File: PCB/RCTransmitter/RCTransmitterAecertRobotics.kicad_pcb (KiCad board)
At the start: 2 copper layers, 141.6 x 101.5 mm, 41 parts, among them J5019_1 J5019 Charger, K1 KCD1 Power Switch, P1 PCF8575

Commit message: updated new design
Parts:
- 10k_Potentiometer1: renamed from ‎PTV09A_1; value R_Potentiometer -> PTV09A-4220F-B103
- 10k_Potentiometer2: renamed from ‎PTV09A_2; value R_Potentiometer -> PTV09A-4220F-B103
- JST_Connector1: renamed from 1.27mm_JST_Connector_1; value Conn_01x02_Socket -> 1.27mm_JST_Connector_1
- Level_Shifter1: renamed from TXS0108E_1; value Level Shifter TXS0108EPW -> TXS0108EPW
- NRF24: renamed from NRF24L01+PA+LNA1; value NRF24L01 -> NRF24L01+PA+LNA1
- Rotary_Encoder1: renamed from EC11E_1; value RotaryEncoder_Switch -> EC11E
- Touch_Screen1: renamed from ILI9488_1; value Screen ILI9488 -> Hosyond 3.5 Inch TFT Touch Screen ILI9488
- moved H8 3.10 mm to (166.4, 67.3)
- renumbered HT7333-A_1 to 3.3V_Regulator1, J5019_1 to Battery_Charger1, KW12_1 to Bumper1, KW12_3 to Bumper2, KW12_2 to Bumper3, KW12_4 to Bumper4, Tact_Push_Button_1 to Button1, Tact_Push_Button_2 to Button2, Tact_Push_Button_3 to Button3, Tact_Push_Button_4 to Button4, MPU6050_1 to Gyroscope1, P1 to IO_Extender1, THB001P_1 to Joystick1, THB001P_2 to Joystick2, SPST_6A_Toggle_Switch_1 to Toggle_Switch1, SPST_6A_Toggle_Switch_2 to Toggle_Switch2, SPST_6A_Toggle_Switch_3 to Toggle_Switch3, SPST_6A_Toggle_Switch_4 to Toggle_Switch4
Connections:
- net /Button A (P03) renamed /Button A
- net /Button B (P04) renamed /Button B
- net /Button C (P05) renamed /Button C
- net /Button D (P06) renamed /Button D
- net /Joy Left Button (P01) renamed /Joy Left Button
- net /Joy Right Button (P02) renamed /Joy Right Button
- net /Left Bumper A (P07) renamed /Left Bumper A
- net /Left Bumper B (P10) renamed /Left Bumper B
- net /Right Bumper A (P11) renamed /Right Bumper A
- net /Right Bumper B (P12) renamed /Right Bumper B
- net /Rotary Encoder Switch (P00) renamed /Rotary Encoder Switch
- net /TFT Reset (D10) renamed /TFT Reset
- net /Toggle A (P13) renamed /Toggle A
- net /Toggle B (P14) renamed /Toggle B
- net /Toggle C (P15) renamed /Toggle C
- net /Toggle D (P16) renamed /Toggle D
- Arduino_Nano_V3 pad 10: /TFT CS (D7) -> /TFT CS
- Arduino_Nano_V3 pad 11: /TFT DC (D8) -> /TFT DC
- Arduino_Nano_V3 pad 12: /Touch Screen CS (D9) -> /Touch Screen CS
- Arduino_Nano_V3 pad 14: /MOSI (D11) -> /MOSI
- Arduino_Nano_V3 pad 15: /MISO (D12) -> /MISO
- Arduino_Nano_V3 pad 16: /SCK (D13) -> /SCK
- Arduino_Nano_V3 pad 19: /Joy Left Y (A0) -> /Joy Left Y
- Arduino_Nano_V3 pad 20: /Joy Left X (A1) -> /Joy Left X
- Arduino_Nano_V3 pad 21: /Pot Left (A6) -> /Pot Left
- Arduino_Nano_V3 pad 22: /Joy Right X (A2) -> /Joy Right X
- Arduino_Nano_V3 pad 23: /SDA (A4) -> /SDA
- Arduino_Nano_V3 pad 24: /SCL (A5) -> /SCL
- Arduino_Nano_V3 pad 25: /Joy Right Y (A3) -> /Joy Right Y
- Arduino_Nano_V3 pad 26: /Pot Right (A7) -> /Pot Right
- Arduino_Nano_V3 pad 5: /RotaryEncoderA (D2) -> /RotaryEncoderA
- Arduino_Nano_V3 pad 6: /RotaryEncoderB (D3) -> /RotaryEncoderB
- Arduino_Nano_V3 pad 8: /NRF CSN (D5) -> /NRF CSN
- Arduino_Nano_V3 pad 9: /NRF CE (D6) -> /NRF CE
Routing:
- net /5v: track 610.6 -> 496.6 mm
- net /TFT Reset: track 112.2 -> 34.5 mm
- net /Pot Right (A7): track 48.3 -> 70.7 mm, vias 3 -> 0
- net /3.3v: track 163.8 -> 182.1 mm, vias 8 -> 6
- net /SDA (A4): track 111.8 -> 98.5 mm, vias 8 -> 6
- net /Pot Left (A6): track 75.8 -> 87.5 mm, vias 5 -> 0
- net /SCL (A5): track 109.4 -> 100.3 mm, vias 8 -> 6
- net /Toggle D: track 105.8 -> 114.3 mm
- net /Joy Left X (A1): track 117.2 -> 124.6 mm
- net /Toggle B: track 50.6 -> 43.5 mm
- net Net-(Battery_Charger1-BAT+): track 62.9 -> 68.5 mm
- net /SCK (D13): track 117.7 -> 122.1 mm, vias 6 -> 7
- net /Toggle A: track 57.6 -> 53.2 mm
- net /Joy Left Y (A0): track 117.1 -> 121.5 mm
- net /Joy Right Button: track 116.0 -> 118.9 mm
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
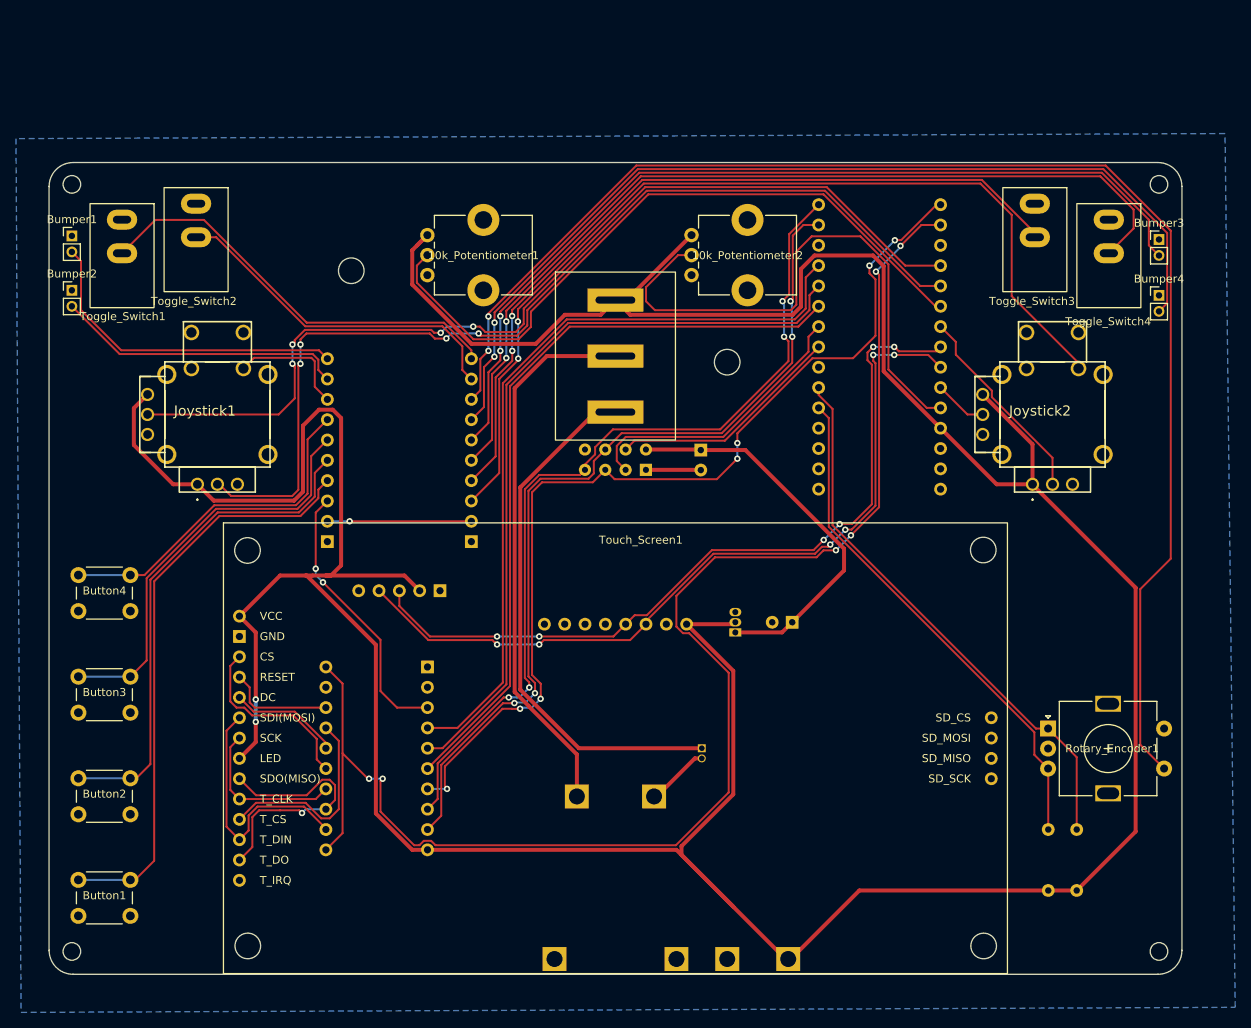
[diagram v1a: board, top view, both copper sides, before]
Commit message: nrf and screen not working at the same time
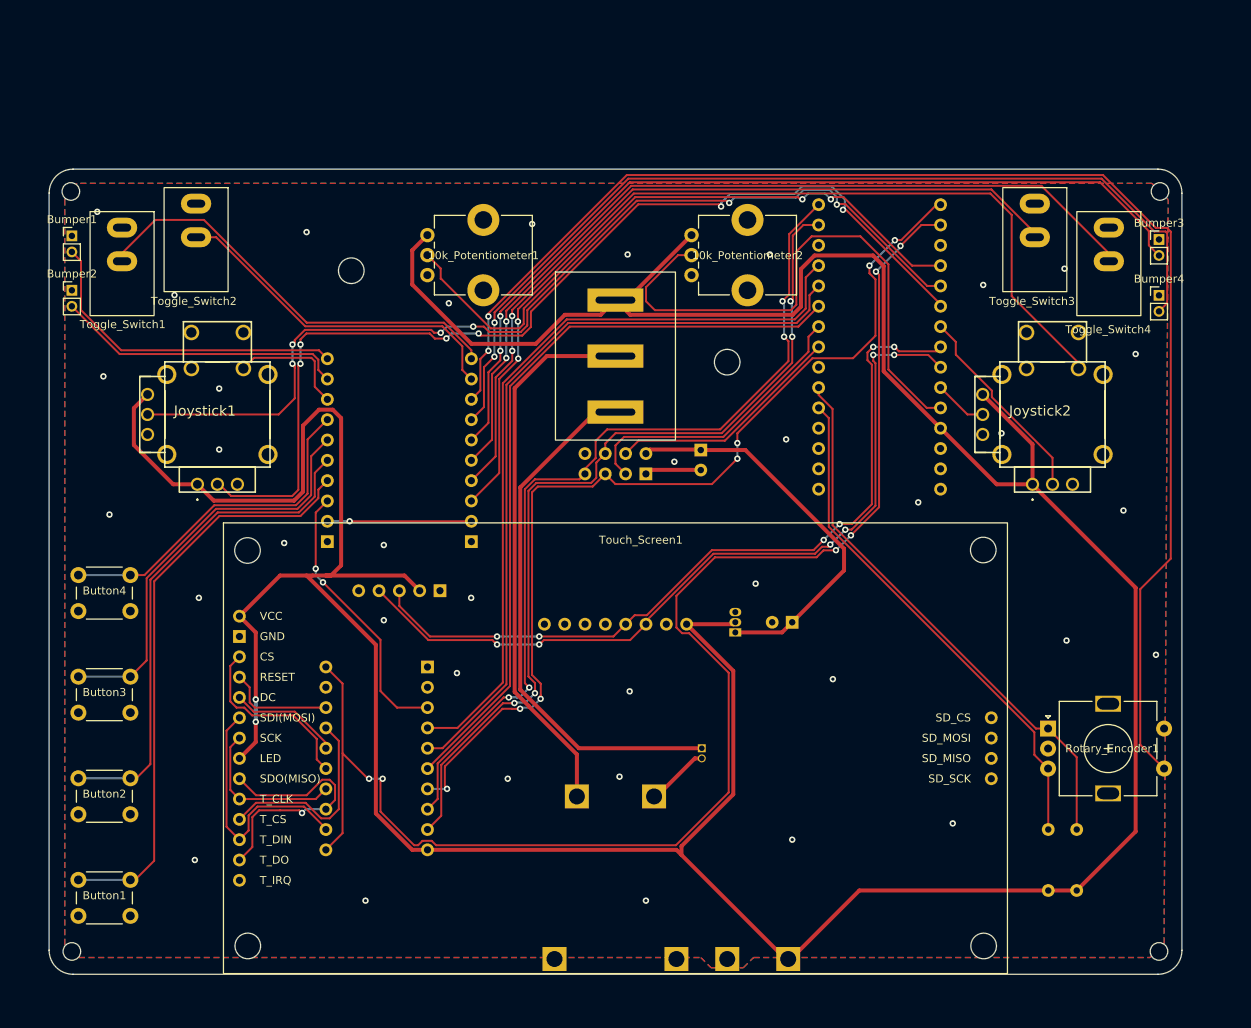
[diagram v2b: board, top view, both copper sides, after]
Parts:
- moved Toggle_Switch1 1.00 mm to (90.7, 48.5)
- moved Toggle_Switch4 1.00 mm to (214.1, 48.5)
- moved H2 0.90 mm to (220.5, 46.0)
- moved H1 0.90 mm to (84.3, 46.0)
- moved NRF24 0.51 mm to (156.2, 81.3)
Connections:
- 10k_Potentiometer1 pad 2: /Pot Left (A6) -> /Pot Left
- 10k_Potentiometer2 pad 2: /Pot Right (A7) -> /Pot Right
- Arduino_Nano_V3 pad 19: /Joy Left Y -> /Pot Left
- Arduino_Nano_V3 pad 20: /Joy Left X -> /Joy Left Y
- Arduino_Nano_V3 pad 21: /Pot Left -> /Joy Left X
- Joystick1 pad 12: /Joy Left Y (A0) -> /Joy Left Y
- Joystick1 pad 2: /Joy Left X (A1) -> /Joy Left X
- Joystick2 pad 12: /Joy Right Y (A3) -> /Joy Right Y
- Joystick2 pad 2: /Joy Right X (A2) -> /Joy Right X
- Level_Shifter1 pad 14: /Touch Screen CS (D9) -> /Touch Screen CS
- Level_Shifter1 pad 15: /TFT DC (D8) -> /TFT DC
- Level_Shifter1 pad 16: /TFT CS (D7) -> /TFT CS
- Level_Shifter1 pad 17: /SCK (D13) -> /SCK
- Level_Shifter1 pad 18: /MISO (D12) -> /MISO
- Level_Shifter1 pad 19: /MOSI (D11) -> /MOSI
- NRF24 pad 2: /NRF CSN (D5) -> /NRF CSN
- NRF24 pad 3: /MOSI (D11) -> /MOSI
- NRF24 pad 5: /MISO (D12) -> /MISO
- NRF24 pad 6: /SCK (D13) -> /SCK
- NRF24 pad 7: /NRF CE (D6) -> /NRF CE
- R10k_1 pad 2: /RotaryEncoderB (D3) -> /RotaryEncoderB
- R10k_2 pad 2: /RotaryEncoderA (D2) -> /RotaryEncoderA
- Rotary_Encoder1 pad A: /RotaryEncoderB (D3) -> /RotaryEncoderB
- Rotary_Encoder1 pad B: /RotaryEncoderA (D2) -> /RotaryEncoderA
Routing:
- net /Joy Left X: track 0.00 -> 127.8 mm, vias 0 -> 6
- net /Joy Left X (A1): track 124.6 -> 0.00 mm, vias 4 -> 0
- net /Joy Left Y: track 0.00 -> 123.0 mm, vias 0 -> 6
- net /SCK: track 0.00 -> 122.2 mm, vias 0 -> 7
- net /SCK (D13): track 122.1 -> 0.00 mm, vias 7 -> 0
- net /Joy Left Y (A0): track 121.5 -> 0.00 mm, vias 4 -> 0
- net /MOSI: track 0.00 -> 111.2 mm, vias 0 -> 4
- net /MOSI (D11): track 110.2 -> 0.00 mm, vias 4 -> 0
- net /MISO: track 0.00 -> 109.6 mm, vias 0 -> 4
- net /MISO (D12): track 108.9 -> 0.00 mm, vias 4 -> 0
- net /Touch Screen CS (D9): track 97.0 -> 0.00 mm
- net /Touch Screen CS: track 0.00 -> 97.0 mm
- net /TFT DC (D8): track 95.9 -> 0.00 mm
- net /TFT DC: track 0.00 -> 95.9 mm
- net /TFT CS (D7): track 94.8 -> 0.00 mm
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- added copper zone on F.Cu, net GND
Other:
- board size 141.6 x 101.5 mm -> 141.6 x 100.6 mm

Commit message: nrf stuff
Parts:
- removed Level_Shifter1: TXS0108EPW, AddedFootprints:HW-221 Level Shifter
- removed Touch_Screen1: Hosyond 3.5 Inch TFT Touch Screen ILI9488, AddedFootprints:3.5 Inch Screen SPI_Module_ILI9488
- added OLED_LCD_Display1: SSD1309 2.4inch, AddedFootprints:OLED LCD Display SSD1309, F.Cu at (116.9, 90.2)
- H1, H10, H2, H9: footprint MountingHole:MountingHole_2.2mm_M2 -> MountingHole:MountingHole_3.2mm_M3
- moved H6 100.7 mm to (219.7, 47.0)
- moved H10 91.4 mm to (168.9, 65.4)
- moved H9 91.1 mm to (135.3, 65.4)
- moved H8 83.8 mm to (85.1, 47.0)
- moved IO_Extender1 75.3 mm to (125.5, 139.9), turned to 0 degrees
- moved H1 57.5 mm to (118.7, 92.1)
- moved H2 57.5 mm to (186.1, 92.1)
- moved C10uf_3 46.8 mm to (135.0, 74.7), turned to 90 degrees
- moved Button1 43.4 mm to (113.1, 98.8)
- moved H5 42.6 mm to (118.9, 131.6)
- moved H7 42.5 mm to (186.1, 131.4)
- moved 3.3V_Regulator1 38.2 mm to (140.1, 74.3)
- moved Button4 37.5 mm to (113.1, 129.2)
- moved Button2 26.0 mm to (113.1, 108.9)
- moved Button3 22.8 mm to (113.1, 119.1)
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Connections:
- 10k_Potentiometer1 pad 3: /5v -> /REF
- 10k_Potentiometer2 pad 3: /5v -> /REF
- 3.3V_Regulator1 pad 2: /5v -> /Vin
- Arduino_Nano_V3 pad 10: /TFT CS -> /Screen RES
- Arduino_Nano_V3 pad 11: /TFT DC -> /Screen DC
- Arduino_Nano_V3 pad 12: /Touch Screen CS -> /Screen CS
- Arduino_Nano_V3 pad 18: unconnected-(Arduino_Nano_V3-AREF-Pad18) -> /REF
- Arduino_Nano_V3 pad 20: /Joy Left Y -> /Pot Right
- Arduino_Nano_V3 pad 21: /Joy Left X -> /Joy Right X
- Arduino_Nano_V3 pad 22: /Joy Right X -> /Joy Right Y
- Arduino_Nano_V3 pad 25: /Joy Right Y -> /Joy Left Y
- Arduino_Nano_V3 pad 26: /Pot Right -> /Joy Left X
- Arduino_Nano_V3 pad 30: unconnected-(Arduino_Nano_V3-VIN-Pad30) -> /Vin
- Battery_Charger1 pad 1: /5v -> /Vin
- Battery_Charger1 pad 2: GND -> Net-(Battery_Charger1-VOUT-)
- Bumper1 pad 1: GND -> /5v
- Bumper2 pad 1: GND -> /5v
- Bumper3 pad 1: GND -> /5v
- Bumper4 pad 1: GND -> /5v
- Button1 pad 1: GND -> /5v
- Button2 pad 1: GND -> /5v
- Button3 pad 1: GND -> /5v
- Button4 pad 1: GND -> /5v
- Gyroscope1 pad 3: /SCL (A5) -> /SCL
- Gyroscope1 pad 4: /SDA (A4) -> /SDA
- IO_Extender1 pad 0: /TFT Reset -> /Joy Left Button
- IO_Extender1 pad 1: /Button A -> /Joy Right Button
- IO_Extender1 pad 10: /Toggle A -> /Button D
- IO_Extender1 pad 11: /Toggle B -> /Button C
- IO_Extender1 pad 12: /Rotary Encoder Switch -> /Button B
- IO_Extender1 pad 13: /Right Bumper B -> /Button A
- IO_Extender1 pad 14: /Right Bumper A -> /Left Bumper A
- IO_Extender1 pad 15: /Toggle D -> /Toggle A
- IO_Extender1 pad 16: /Toggle C -> /Toggle B
- IO_Extender1 pad 17: /Joy Right Button -> /Left Bumper B
- IO_Extender1 pad 2: /Button B -> /Toggle C
- IO_Extender1 pad 21: /SDA (A4) -> /SDA
- IO_Extender1 pad 22: /SCL (A5) -> /SCL
- IO_Extender1 pad 3: /Button C -> /Toggle D
- IO_Extender1 pad 4: /Button D -> /Right Bumper B
- IO_Extender1 pad 5: /Joy Left Button -> /Right Bumper A
- IO_Extender1 pad 6: /Left Bumper B -> /Rotary Encoder Switch
- IO_Extender1 pad 7: /Left Bumper A -> unconnected-(IO_Extender1-P07-Pad7)
- JST_Connector1 pad 1: Net-(JST_Connector1-Pin_1) -> Net-(Battery_Charger1-BAT+)
- K1 pad 1: /5v -> GND
- K1 pad 2: Net-(Battery_Charger1-BAT+) -> Net-(Battery_Charger1-VOUT-)
- K1 pad 3: Net-(JST_Connector1-Pin_1) -> /Vin
- Toggle_Switch1 pad 1: GND -> /5v
- Toggle_Switch2 pad 1: GND -> /5v
- Toggle_Switch3 pad 1: GND -> /5v
- Toggle_Switch4 pad 1: GND -> /5v
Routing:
- net /3.3v: track 182.1 -> 0.00 mm, vias 6 -> 0
- net /Vin: track 0.00 -> 144.2 mm, vias 0 -> 3
- net /Rotary Encoder Switch: track 176.9 -> 76.0 mm
- net /SCL (A5): track 100.3 -> 0.00 mm, vias 6 -> 0
- net /SDA (A4): track 98.5 -> 0.00 mm, vias 6 -> 0
- net Net-(Battery_Charger1-VOUT-): track 0.00 -> 97.2 mm, vias 0 -> 2
- net /Touch Screen CS: track 97.0 -> 0.00 mm
- net /TFT DC: track 95.9 -> 0.00 mm
- net /TFT CS: track 94.8 -> 0.00 mm
- net /REF: track 0.00 -> 93.5 mm
- net /SDA: track 0.00 -> 85.0 mm, vias 0 -> 2
- net /SCL: track 0.00 -> 80.8 mm, vias 0 -> 2
- net /5v: track 485.5 -> 416.8 mm, vias 2 -> 0
- net /Left Bumper A: track 41.1 -> 108.8 mm, vias 0 -> 2
- net /Screen CS: track 0.00 -> 67.4 mm
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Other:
- board size 141.6 x 100.6 mm -> 142.2 x 100.6 mm
